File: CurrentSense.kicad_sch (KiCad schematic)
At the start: 4 parts, among them J3 XT60PW-M, U4 INA181A3IDBVR

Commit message: fixed schematic a little
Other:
- note added: "I_max = 15A P = 15^2(0.002)= 0.45W"
- note added: "gain: 100v/v v_shunt = IR = 15*0.002 = 0.03V v_out of current sense amp = gain*v_shunt = 3V v_max of ADC is 3V3 > 3V"
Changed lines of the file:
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@@
 	(generator_version "10.0")
 	(paper "A4")
+	(text "gain: 100v/v\nv_shunt = IR = 15*0.002 = 0.03V\nv_out of current sense amp = gain*v_shunt = 3V\nv_max of ADC is 3V3 > 3V\n"
+		(exclude_from_sim no)
+		(at 57.15 93.726 0)
+		(effects
+			(font
+				(size 1.27 1.27)
+			)
+		)
+	)
+	(text "I_max = 15A\nP = 15^2(0.002)= 0.45W"
+		(exclude_from_sim no)
+		(at 57.658 103.378 0)
+		(effects
+			(font
+				(size 1.27 1.27)
+			)
+		)
+	)
 	(junction
 		(at 125.73 97.79)

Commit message: damir review
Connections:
- net 48V: now also J3.1 (P); no longer R12.1, U4.3 (IN+)
- net GND: now also R12.2, U4.4 (IN-); no longer J3.2 (N), J3.SH1 (SHIELD), J3.SH2 (SHIELD)
- new net: J3.2 (N), J3.SH1 (SHIELD), J3.SH2 (SHIELD), R12.1, U4.3 (IN+)

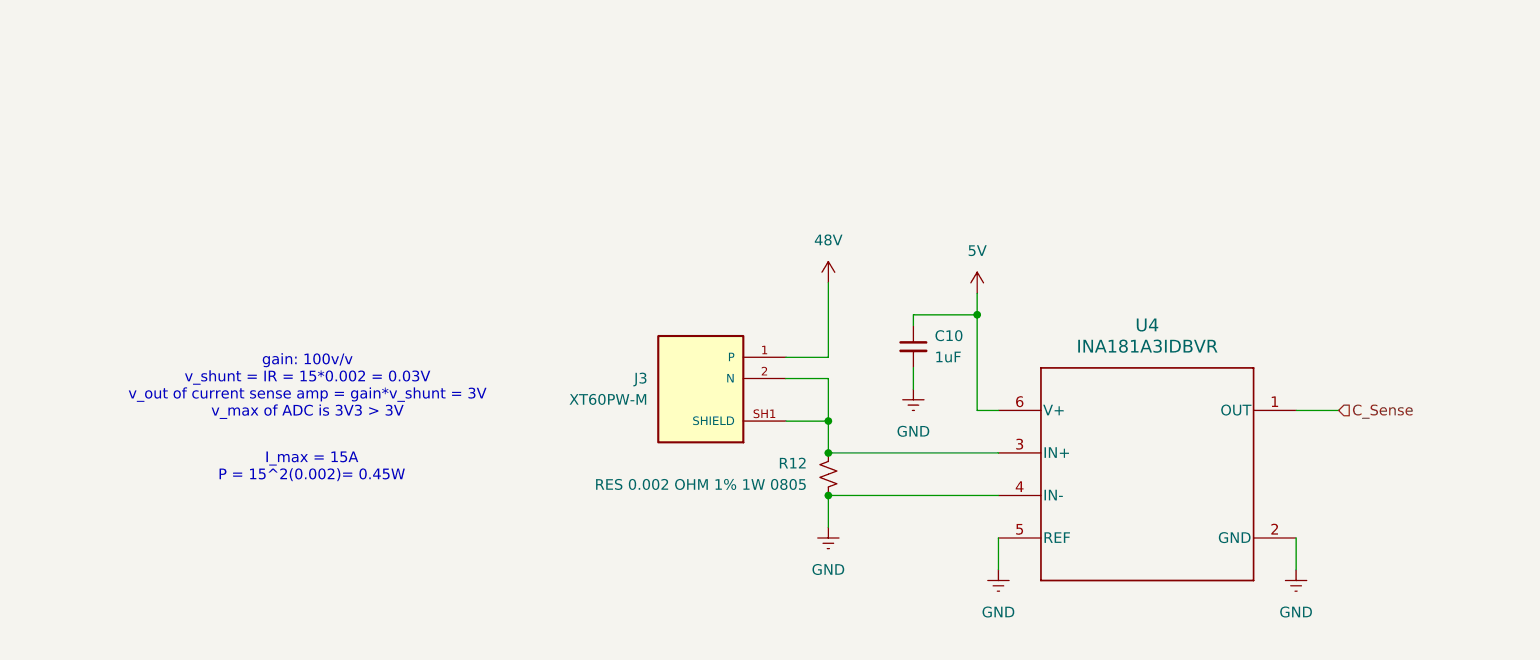
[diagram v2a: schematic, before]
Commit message: fixed csense connectors and stm
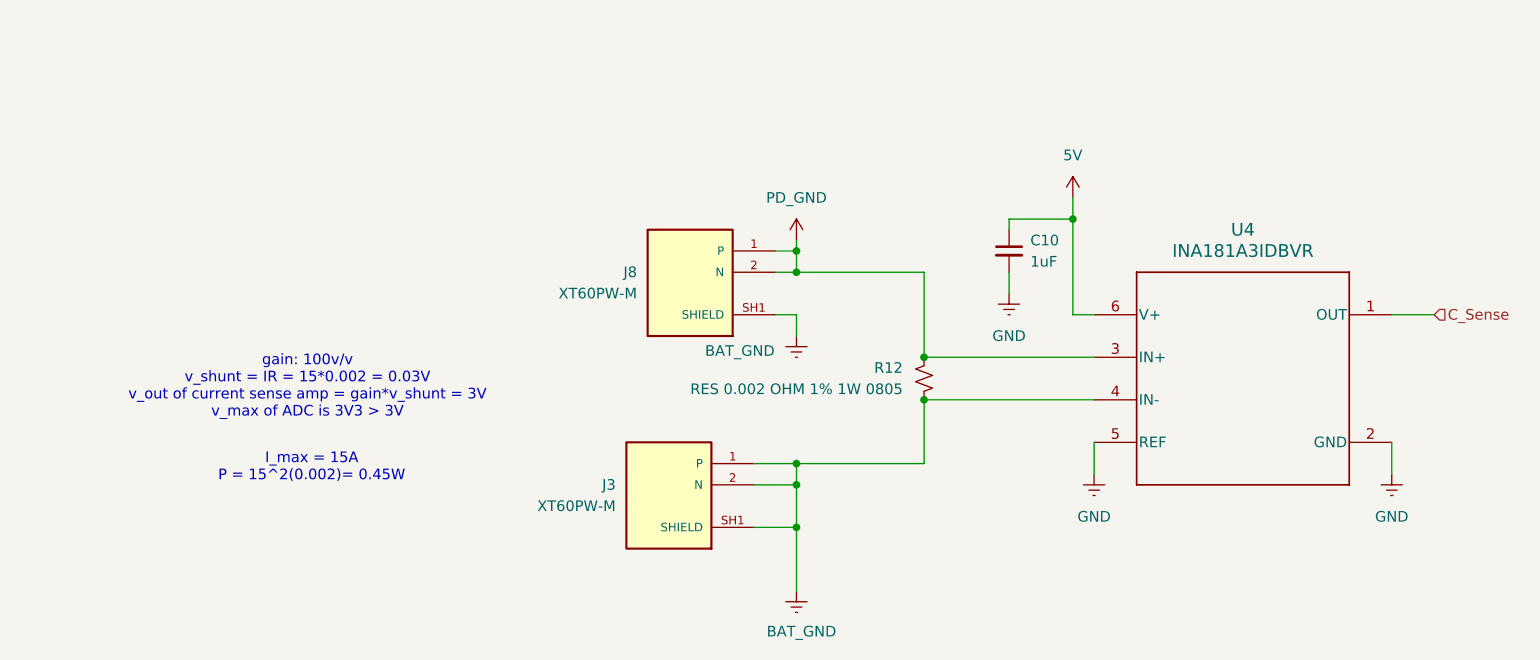
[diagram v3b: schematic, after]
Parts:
- added J8: XT60PW-M, footprints:AMASS_XT60PW-M, symbol symbols:XT60PW-M
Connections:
- net 48V is gone; now on net BAT_GND: J3.1 (P)
- net GND: no longer R12.2, U4.4 (IN-)
- net BAT_GND: now reaches J3.2 (N), J3.SH1 (SHIELD), J3.SH2 (SHIELD)
- net BAT_GND: now also R12.2, U4.4 (IN-), J8.SH1 (SHIELD), J8.SH2 (SHIELD); no longer R12.1, U4.3 (IN+)
- new net PD_GND: J8.1 (P), J8.2 (N), R12.1, U4.3 (IN+)
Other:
- moved on the sheet: J3

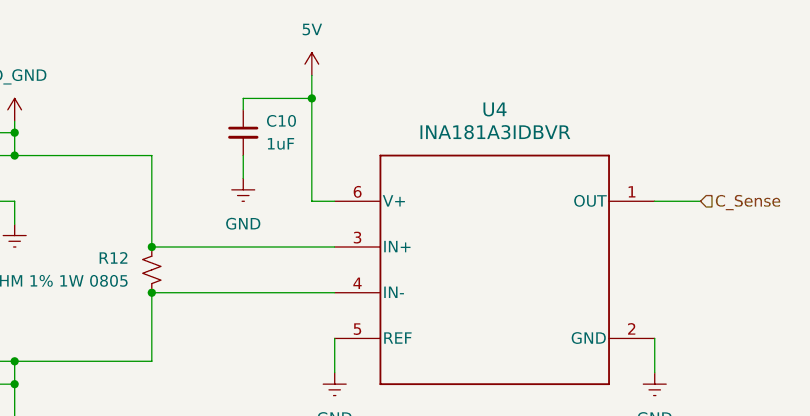
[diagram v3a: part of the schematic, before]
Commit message: added passives
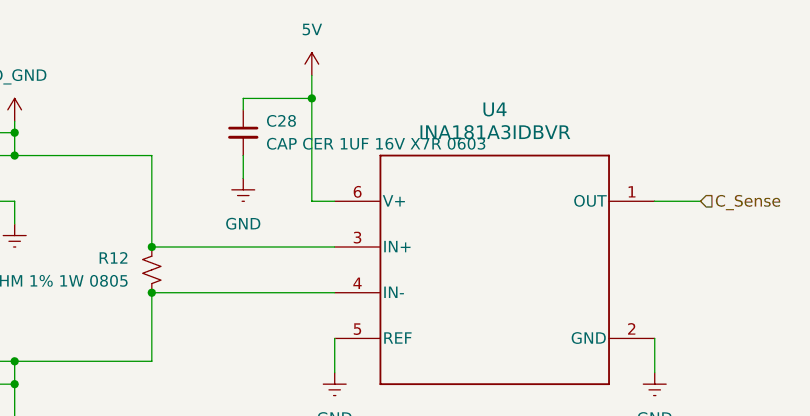
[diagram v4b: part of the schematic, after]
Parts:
- removed C10: 1uF, symbol Device:C_Small
- added C28: CAP CER 1UF 16V X7R 0603, Capacitor_SMD:C_0603_1608Metric, symbol Device:C_Small
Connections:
- net 5V: now also C28.1
- net GND: now also C28.2
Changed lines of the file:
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@@
 		(dnp no)
 		(fields_autoplaced yes)
-		(property "Reference" "C10"
+		(property "Reference" "C28"
 			(at 149.86 90.1762 0)
 			(show_name no)
@@
 			)
 		)
-		(property "Value" "1uF"
+		(property "Value" "CAP CER 1UF 16V X7R 0603"
 			(at 149.86 92.7162 0)
 			(show_name no)
@@
 			)
 		)
-		(property "Footprint" ""
+		(property "Footprint" "Capacitor_SMD:C_0603_1608Metric"
 			(at 147.32 91.44 0)
 			(hide yes)
@@
 			)
 		)
-		(property "Datasheet" ""
+		(property "Datasheet" "https://www.digikey.ca/en/products/detail/kemet/C0603C105K4RACTU/2199788"
 			(at 147.32 91.44 0)
 			(hide yes)
@@
 			)
 		)
-		(property "Description" "Unpolarized capacitor, small symbol"
+		(property "Description" "1 µF ±10% 16V Ceramic Capacitor X7R 0603 (1608 Metric)"
 			(at 147.32 91.44 0)
 			(hide yes)
@@
 			)
 		)
+		(pin "2"
+		)
 		(pin "1"
-		)
-		(pin "2"
 		)
 		(instances
 			(project "bms-main"
 				(path "/d7e1c873-142c-4805-8303-47f5b9830fe8/fcf0b0b9-3f68-46bd-a825-62168094e731"
-					(reference "C10")
+					(reference "C28")
 					(unit 1)
 				)

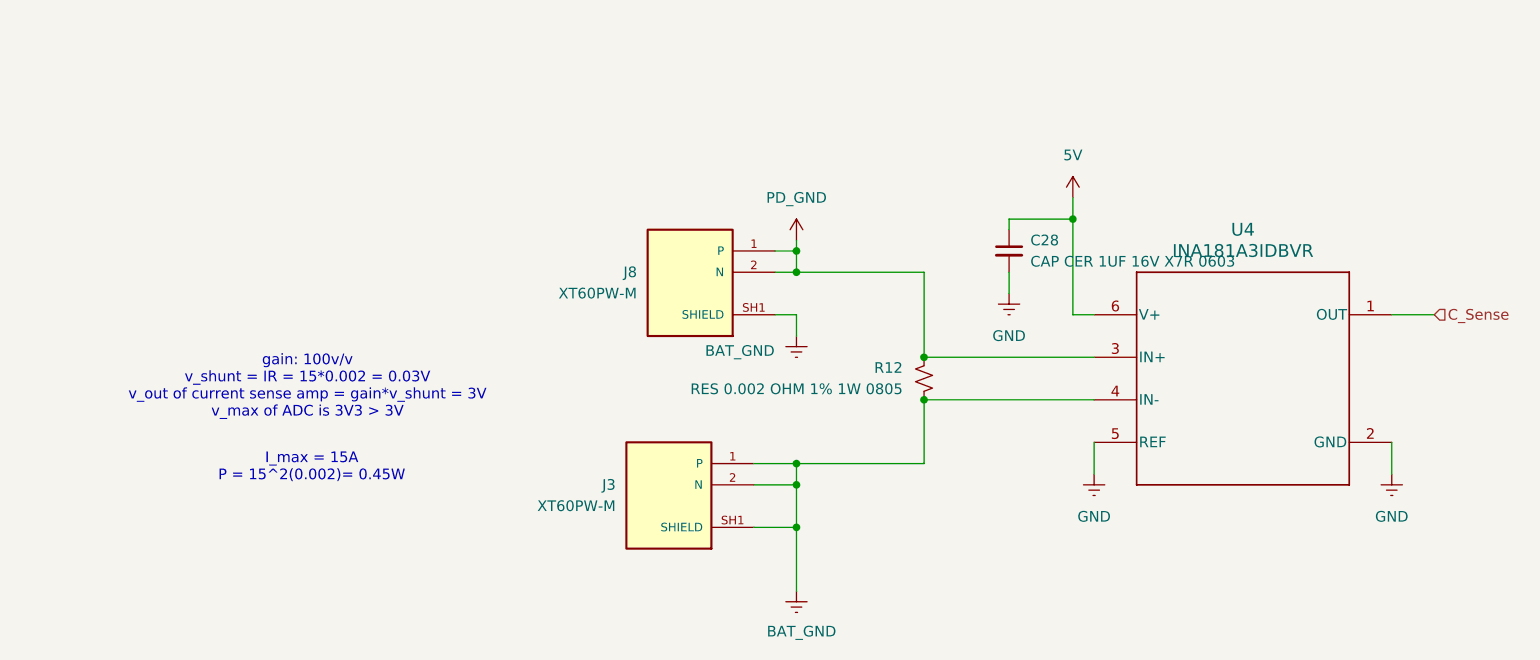
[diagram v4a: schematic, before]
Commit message: cleaned up schematic
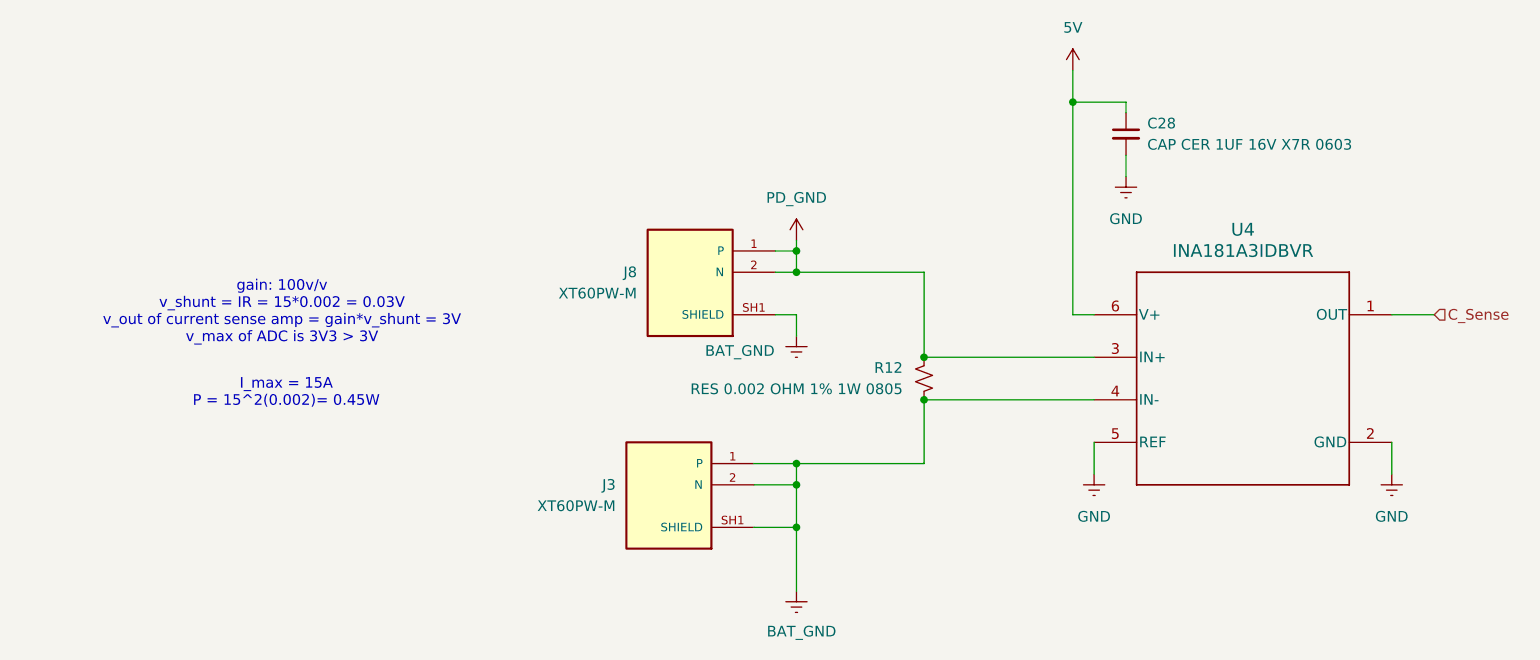
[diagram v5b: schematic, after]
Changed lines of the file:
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@@
 	(text "gain: 100v/v\nv_shunt = IR = 15*0.002 = 0.03V\nv_out of current sense amp = gain*v_shunt = 3V\nv_max of ADC is 3V3 > 3V\n"
 		(exclude_from_sim no)
-		(at 63.5 107.696 0)
+		(at 60.452 98.806 0)
 		(effects
 			(font
@@
 	(text "I_max = 15A\nP = 15^2(0.002)= 0.45W"
 		(exclude_from_sim no)
-		(at 64.008 117.348 0)
+		(at 60.96 108.458 0)
 		(effects
 			(font
@@
 	)
 	(junction
-		(at 154.94 87.63)
-		(diameter 0)
-		(color 0 0 0 0)
-	)
-	(junction
 		(at 137.16 109.22)
 		(diameter 0)
@@
 	)
 	(junction
+		(at 154.94 73.66)
+		(diameter 0)
+		(color 0 0 0 0)
+	)
+	(junction
 		(at 121.92 91.44)
 		(diameter 0)
@@
 	(wire
 		(pts
+			(xy 161.29 74.93) (xy 161.29 73.66)
+		)
+		(stroke
+			(width 0)
+			(type default)
+		)
+	)
+	(wire
+		(pts
 			(xy 116.84 119.38) (xy 121.92 119.38)
 		)
@@
 	(wire
 		(pts
-			(xy 154.94 85.09) (xy 154.94 87.63)
-		)
-		(stroke
-			(width 0)
-			(type default)
-		)
-	)
-	(wire
-		(pts
 			(xy 119.38 91.44) (xy 121.92 91.44)
 		)
@@
 	(wire
 		(pts
+			(xy 154.94 99.06) (xy 157.48 99.06)
+		)
+		(stroke
+			(width 0)
+			(type default)
+		)
+	)
+	(wire
+		(pts
 			(xy 157.48 114.3) (xy 157.48 118.11)
 		)
@@
 	(wire
 		(pts
+			(xy 154.94 73.66) (xy 154.94 99.06)
+		)
+		(stroke
+			(width 0)
+			(type default)
+		)
+	)
+	(wire
+		(pts
 			(xy 137.16 116.84) (xy 137.16 109.22)
 		)
@@
 	(wire
 		(pts
-			(xy 154.94 87.63) (xy 154.94 99.06)
-		)
-		(stroke
-			(width 0)
-			(type default)
-		)
-	)
-	(wire
-		(pts
-			(xy 154.94 99.06) (xy 157.48 99.06)
-		)
-		(stroke
-			(width 0)
-			(type default)
-		)
-	)
-	(wire
-		(pts
-			(xy 147.32 87.63) (xy 154.94 87.63)
-		)
-		(stroke
-			(width 0)
-			(type default)
-		)
-	)
-	(wire
-		(pts
-			(xy 147.32 93.98) (xy 147.32 96.52)
+			(xy 154.94 69.85) (xy 154.94 73.66)
+		)
+		(stroke
+			(width 0)
+			(type default)
+		)
+	)
+	(wire
+		(pts
+			(xy 161.29 80.01) (xy 161.29 82.55)
 		)
 		(stroke
@@
 	(wire
 		(pts
-			(xy 147.32 88.9) (xy 147.32 87.63)
+			(xy 154.94 73.66) (xy 161.29 73.66)
 		)
 		(stroke
@@
 				(path "/d7e1c873-142c-4805-8303-47f5b9830fe8/fcf0b0b9-3f68-46bd-a825-62168094e731"
 					(reference "U4")
-					(unit 1)
-				)
-			)
-		)
-	)
-	(symbol
-		(lib_id "power:GNDREF")
-		(at 147.32 96.52 0)
-		(unit 1)
-		(body_style 1)
-		(exclude_from_sim no)
-		(in_bom yes)
-		(on_board yes)
-		(in_pos_files yes)
-		(dnp no)
-		(fields_autoplaced yes)
-		(property "Reference" "#PWR033"
-			(at 147.32 102.87 0)
-			(hide yes)
-			(show_name no)
-			(do_not_autoplace no)
-			(effects
-				(font
-					(size 1.27 1.27)
-				)
-			)
-		)
-		(property "Value" "GND"
-			(at 147.32 101.6 0)
-			(show_name no)
-			(do_not_autoplace no)
-			(effects
-				(font
-					(size 1.27 1.27)
-				)
-			)
-		)
-		(property "Footprint" ""
-			(at 147.32 96.52 0)
-			(hide yes)
-			(show_name no)
-			(do_not_autoplace no)
-			(effects
-				(font
-					(size 1.27 1.27)
-				)
-			)
-		)
-		(property "Datasheet" ""
-			(at 147.32 96.52 0)
-			(hide yes)
-			(show_name no)
-			(do_not_autoplace no)
-			(effects
-				(font
-					(size 1.27 1.27)
-				)
-			)
-		)
-		(property "Description" "Power symbol creates a global label with name \"GNDREF\" , reference supply ground"
-			(at 147.32 96.52 0)
-			(hide yes)
-			(show_name no)
-			(do_not_autoplace no)
-			(effects
-				(font
-					(size 1.27 1.27)
-				)
-			)
-		)
-		(pin "1"
-		)
-		(instances
-			(project "bms-main"
-				(path "/d7e1c873-142c-4805-8303-47f5b9830fe8/fcf0b0b9-3f68-46bd-a825-62168094e731"
-					(reference "#PWR033")
 					(unit 1)
 				)
@@
 	)
 	(symbol
+		(lib_id "power:GNDREF")
+		(at 161.29 82.55 0)
+		(unit 1)
+		(body_style 1)
+		(exclude_from_sim no)
+		(in_bom yes)
+		(on_board yes)
+		(in_pos_files yes)
+		(dnp no)
+		(fields_autoplaced yes)
+		(property "Reference" "#PWR033"
+			(at 161.29 88.9 0)
+			(hide yes)
+			(show_name no)
+			(do_not_autoplace no)
+			(effects
+				(font
+					(size 1.27 1.27)
+				)
+			)
+		)
+		(property "Value" "GND"
+			(at 161.29 87.63 0)
+			(show_name no)
+			(do_not_autoplace no)
+			(effects
+				(font
+					(size 1.27 1.27)
+				)
+			)
+		)
+		(property "Footprint" ""
+			(at 161.29 82.55 0)
+			(hide yes)
+			(show_name no)
+			(do_not_autoplace no)
+			(effects
+				(font
+					(size 1.27 1.27)
+				)
+			)
+		)
+		(property "Datasheet" ""
+			(at 161.29 82.55 0)
+			(hide yes)
+			(show_name no)
+			(do_not_autoplace no)
+			(effects
+				(font
+					(size 1.27 1.27)
+				)
+			)
+		)
+		(property "Description" "Power symbol creates a global label with name \"GNDREF\" , reference supply ground"
+			(at 161.29 82.55 0)
+			(hide yes)
+			(show_name no)
+			(do_not_autoplace no)
+			(effects
+				(font
+					(size 1.27 1.27)
+				)
+			)
+		)
+		(pin "1"
+		)
+		(instances
+			(project "bms-main"
+				(path "/d7e1c873-142c-4805-8303-47f5b9830fe8/fcf0b0b9-3f68-46bd-a825-62168094e731"
+					(reference "#PWR033")
+					(unit 1)
+				)
+			)
+		)
+	)
+	(symbol
 		(lib_id "Device:C_Small")
-		(at 147.32 91.44 0)
+		(at 161.29 77.47 0)
 		(unit 1)
 		(body_style 1)
@@
 		(fields_autoplaced yes)
 		(property "Reference" "C28"
-			(at 149.86 90.1762 0)
+			(at 163.83 76.2062 0)
 			(show_name no)
 			(do_not_autoplace no)
@@
 		)
 		(property "Value" "CAP CER 1UF 16V X7R 0603"
-			(at 149.86 92.7162 0)
+			(at 163.83 78.7462 0)
 			(show_name no)
 			(do_not_autoplace no)
@@
 		)
 		(property "Footprint" "Capacitor_SMD:C_0603_1608Metric"
-			(at 147.32 91.44 0)
+			(at 161.29 77.47 0)
 			(hide yes)
 			(show_name no)
@@
 		)
 		(property "Datasheet" "https://www.digikey.ca/en/products/detail/kemet/C0603C105K4RACTU/2199788"
-			(at 147.32 91.44 0)
+			(at 161.29 77.47 0)
 			(hide yes)
 			(show_name no)
@@
 		)
 		(property "Description" "1 µF ±10% 16V Ceramic Capacitor X7R 0603 (1608 Metric)"
-			(at 147.32 91.44 0)
+			(at 161.29 77.47 0)
 			(hide yes)
 			(show_name no)
@@
 	(symbol
 		(lib_id "power:+5V")
-		(at 154.94 85.09 0)
+		(at 154.94 69.85 0)
 		(unit 1)
 		(body_style 1)
@@
 		(fields_autoplaced yes)
 		(property "Reference" "#PWR032"
-			(at 154.94 88.9 0)
+			(at 154.94 73.66 0)
 			(hide yes)
 			(show_name no)
@@
 		)
 		(property "Value" "5V"
-			(at 154.94 80.01 0)
+			(at 154.94 64.77 0)
 			(show_name no)
 			(do_not_autoplace no)
@@
 		)
 		(property "Footprint" ""
-			(at 154.94 85.09 0)
+			(at 154.94 69.85 0)
 			(hide yes)
 			(show_name no)
@@
 		)
 		(property "Datasheet" ""
-			(at 154.94 85.09 0)
+			(at 154.94 69.85 0)
 			(hide yes)
 			(show_name no)
@@
 		)
 		(property "Description" "Power symbol creates a global label with name \"+5V\""
-			(at 154.94 85.09 0)
-			(hide yes)
-			(show_name no)
+			(at 154.94 69.85 0)
+			(hide yes)
+			(show_name no)
